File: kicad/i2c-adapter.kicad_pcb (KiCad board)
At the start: 2 copper layers, 93 x 65 mm, 41 parts, among them J1 Conn_02x13_Top_Bottom, J10 AUX IN, J11 +5V, J2 I2C-1, J3 I2C-2, J4 I2C-3R, J5 I2C-4R, J6 SPI-1, J7 SPI-2, J8 SPI-3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

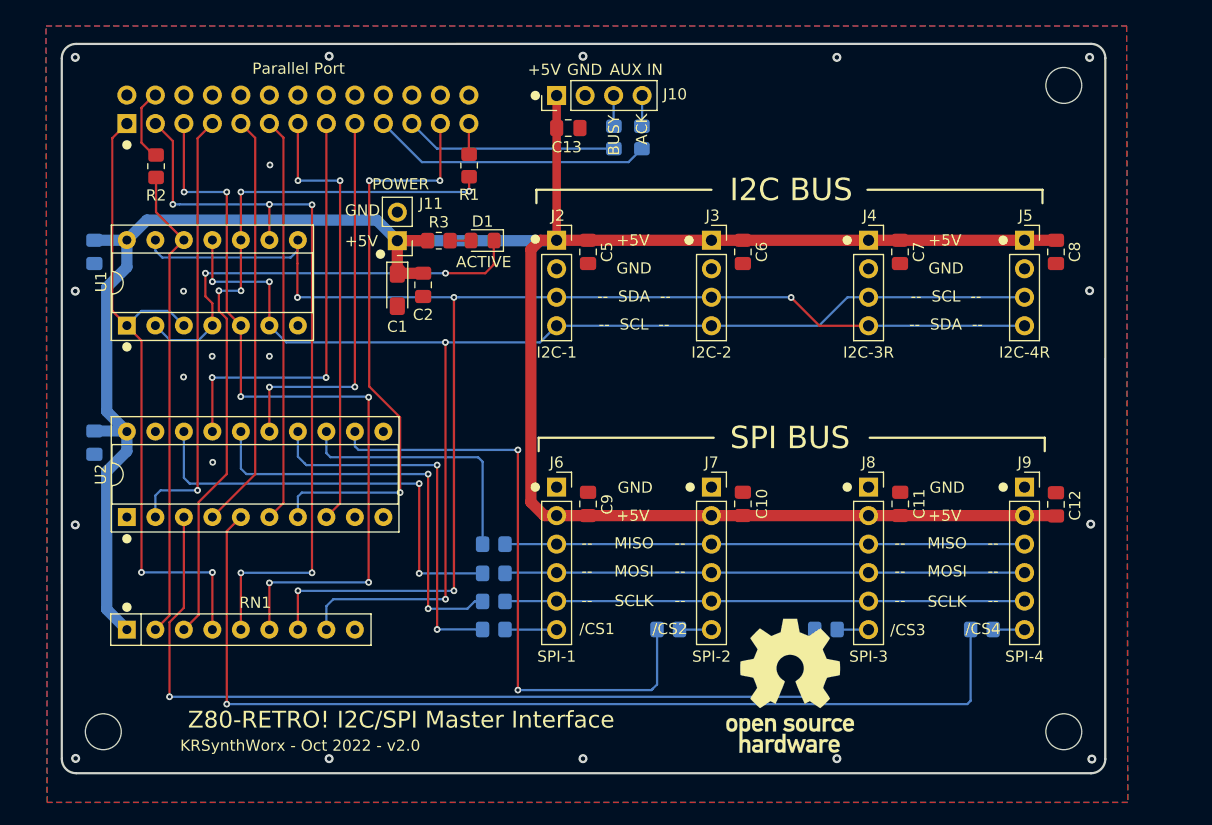
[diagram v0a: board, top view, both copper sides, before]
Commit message: Cleaned up PCB routes and positions; Converted I2C to Adafruit standard pinout. Have Git ignore Kicad generated files.
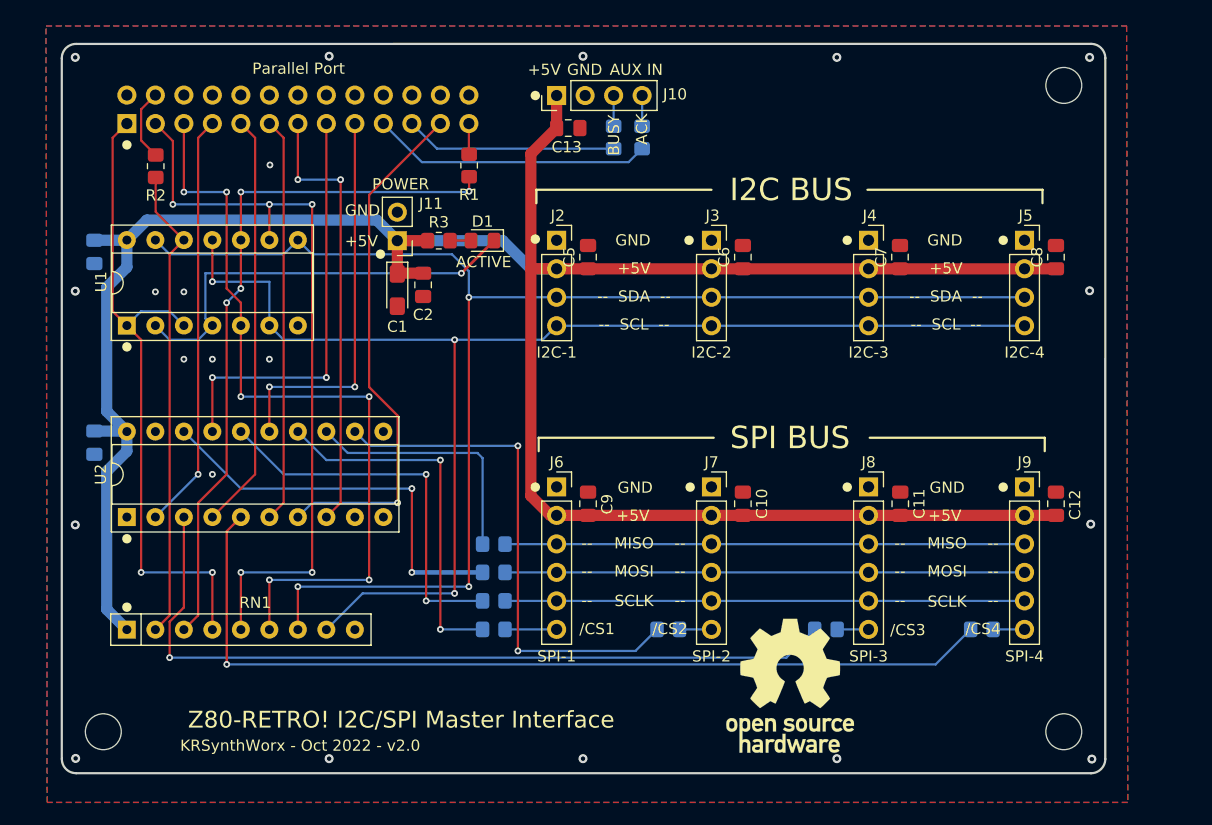
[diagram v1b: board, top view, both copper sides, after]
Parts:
- J1: footprint jb-footprint:PinSocket_2x13_P2.54mm_Vertical_clockwise -> Connector_PinSocket_2.54mm:PinSocket_2x13_P2.54mm_Vertical
- J4: value I2C-3R -> I2C-3
- J5: value I2C-4R -> I2C-4
- moved C5 0.47 mm to (147.9, 83.9), turned to 90 degrees
- moved C6 0.47 mm to (161.7, 83.9), turned to 90 degrees
- moved C7 0.47 mm to (175.7, 83.9), turned to 90 degrees
- moved C8 0.47 mm to (189.6, 83.9), turned to 90 degrees
- moved R7 0.09 mm to (139.5, 112.0)
- moved C12 0.06 mm to (189.6, 105.9)
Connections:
- J2 pad 1: +5V -> GND
- J2 pad 2: GND -> +5V
- J3 pad 1: +5V -> GND
- J3 pad 2: GND -> +5V
- J4 pad 1: +5V -> GND
- J4 pad 2: GND -> +5V
- J4 pad 3: /SCL -> /SDA
- J4 pad 4: /SDA -> /SCL
- J5 pad 1: +5V -> GND
- J5 pad 2: GND -> +5V
- J5 pad 3: /SCL -> /SDA
- J5 pad 4: /SDA -> /SCL
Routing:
- net Net-(U2-Pad5): track 90.0 -> 81.2 mm
- net Net-(U2-Pad12): track 54.9 -> 46.5 mm
- net Net-(U2-Pad3): track 79.8 -> 71.6 mm
- net /PAPER: track 51.4 -> 46.9 mm, vias 3 -> 1
- net Net-(U2-Pad16): track 37.3 -> 34.4 mm
- net +5V: track 220.5 -> 223.3 mm
- net Net-(U2-Pad18): track 39.0 -> 36.2 mm
- net /SDA: track 129.5 -> 126.8 mm, vias 5 -> 3
- net /SCL: track 118.1 -> 116.2 mm, vias 4 -> 3
- net /D2: track 39.1 -> 37.2 mm
- net Net-(R1-Pad2): track 64.5 -> 62.7 mm
- net Net-(D1-Pad1): track 39.2 -> 38.0 mm, vias 2 -> 1
- net Net-(U2-Pad14): track 33.7 -> 32.6 mm
- net Net-(U2-Pad13): track 23.5 -> 22.6 mm
- net GND: vias 20 -> 21

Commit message: Add voltage regulator for +3.3V power; Move all SMD components to top side.
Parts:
- added C14: 10uF, Capacitor_SMD:C_0805_2012Metric_Pad1.18x1.45mm_HandSolder, F.Cu at (161.7, 72.4)
- added C15: .1, Capacitor_SMD:C_0805_2012Metric_Pad1.18x1.45mm_HandSolder, F.Cu at (166.5, 75.9)
- added C16: 10uF, Capacitor_SMD:C_0805_2012Metric_Pad1.18x1.45mm_HandSolder, F.Cu at (175.7, 72.1)
- added REF1: Fiducial_0.5mm_Mask1.5mm, Fiducial:Fiducial_0.5mm_Mask1.5mm, F.Cu at (186.4, 68.6)
- added REF2: Fiducial_0.5mm_Mask1.5mm, Fiducial:Fiducial_0.5mm_Mask1.5mm, F.Cu at (108.7, 126.2)
- added U3: LM1117-3.3, digikey-footprints:SOT-223, F.Cu at (168.7, 71.1)
- C3, C4, R10, R11, R12, R4, R5, R6, R7, R8, R9: moved to F.Cu
- moved C6 1.47 mm to (162.7, 84.9), turned to 0 degrees
- moved REF** 1.34 mm to (165.9, 123.4)
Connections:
- C11 pad 1: +5V -> +3V3
- C12 pad 1: +5V -> +3V3
- C7 pad 1: +5V -> +3V3
- C8 pad 1: +5V -> +3V3
- J4 pad 2: +5V -> +3V3
- J5 pad 2: +5V -> +3V3
- J8 pad 2: +5V -> +3V3
- J9 pad 2: +5V -> +3V3
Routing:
- net +3V3: track 0.00 -> 83.6 mm
- net +5V: track 223.3 -> 185.6 mm
- net /SCL: track 116.2 -> 111.6 mm, vias 3 -> 2
- net /SDA: track 126.8 -> 123.7 mm
- net Net-(R9-Pad1): track 32.6 -> 30.7 mm, vias 2 -> 1
- net Net-(R10-Pad1): track 46.5 -> 44.7 mm, vias 2 -> 1
- net Net-(R8-Pad1): track 34.4 -> 32.9 mm, vias 2 -> 1
- net Net-(R7-Pad1): track 36.2 -> 35.1 mm, vias 2 -> 1
- net Net-(R6-Pad2): track 22.6 -> 21.7 mm, vias 0 -> 1
- net /ACK: track 25.0 -> 24.8 mm, vias 0 -> 1
- net /BUSY: vias 0 -> 1
- net Net-(R11-Pad1): vias 1 -> 0
- net GND: vias 21 -> 33
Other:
- board text added: "+3.3V"
- board text added: "KRSynthWorx - Oct 2022 - v2.1"
- board text removed: "KRSynthWorx - Oct 2022 - v2.0"

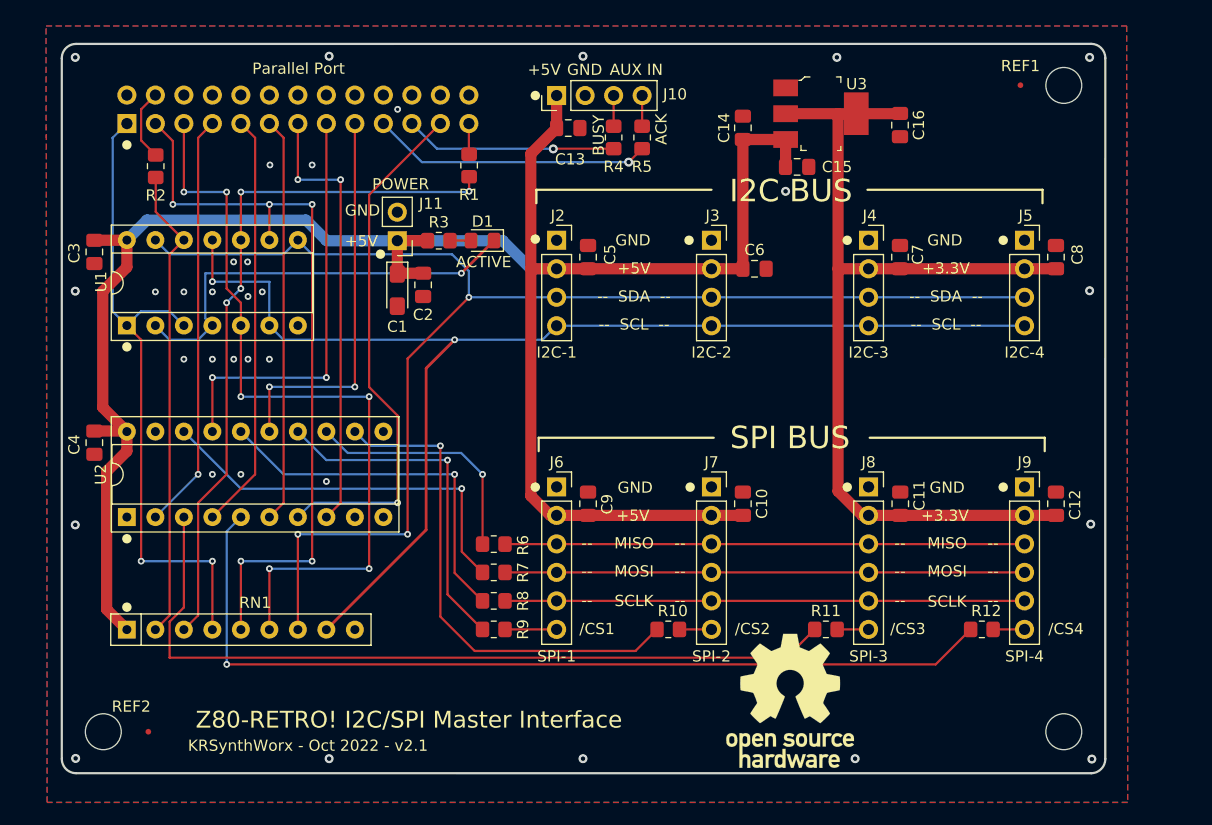
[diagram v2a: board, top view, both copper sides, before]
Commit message: Added BOM; Updated README to point to BOM Added JLCPCB SMD part references Specified LED characteristics (choose whichever color you want, default is RED) For jlcpcb/project.db, see https://github.com/Bouni/kicad-jlcpcb-tools Some minor Schematic and routing cleanups. Removed *_prl preferences file.  It is auto generated upon opening project.
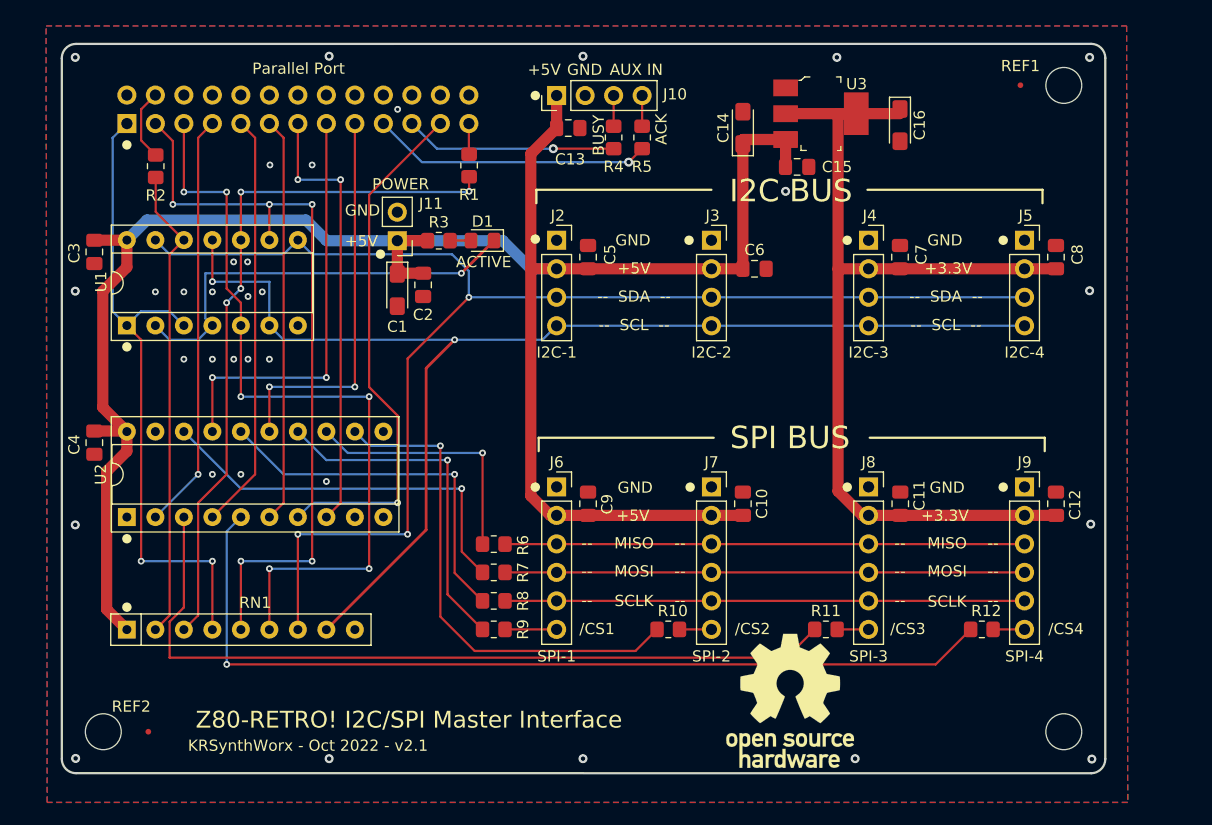
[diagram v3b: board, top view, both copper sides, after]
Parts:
- C1: value 10uf -> 10uF
- C14, C16: footprint Capacitor_SMD:C_0805_2012Metric_Pad1.18x1.45mm_HandSolder -> Capacitor_Tantalum_SMD:CP_EIA-3216-10_Kemet-I_Pad1.58x1.35mm_HandSolder
- C15: value .1 -> 0.1uF
- C2, C3, C4: value 0.1uf -> 0.1uF
- D1: value ACTIVE -> 20mA 120°
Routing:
- net Net-(R6-Pad2): track 21.7 -> 22.8 mm

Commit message: Added Adafruit compatible STEMMA QT I2C Connector and EyeSPI connector.
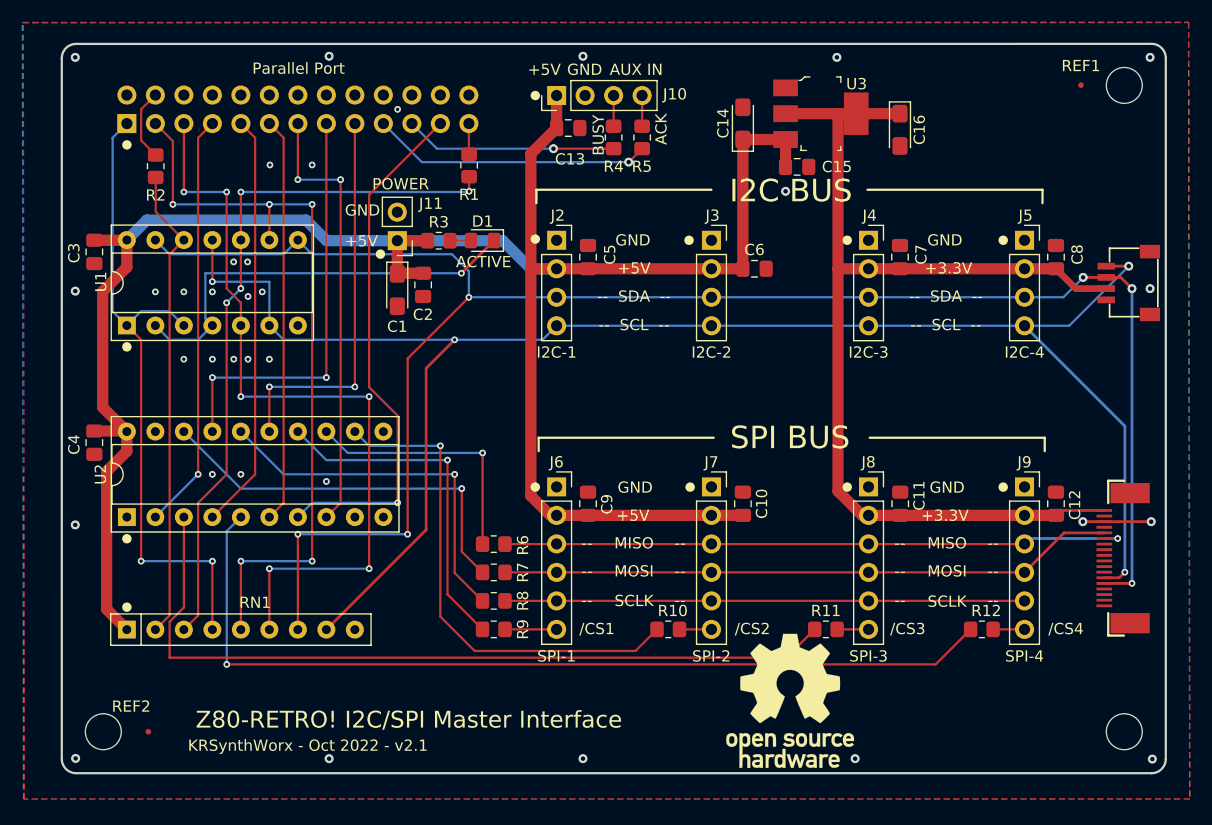
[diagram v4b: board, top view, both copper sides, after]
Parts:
- added CONN1: STEMMA_I2C_QT, i2c-adapter:JST_SH4, F.Cu at (196.6, 86.2)
- added X1: EYE_SPI_DISPLAY_FLIP, i2c-adapter:EYE_SPI_DISPLAY_BOTCONTACT, F.Cu at (195.1, 110.7)
- J1: footprint Connector_PinSocket_2.54mm:PinSocket_2x13_P2.54mm_Vertical -> i2c-adapter:PinSocket_2x13_P2.54mm_Vertical
- U3: footprint digikey-footprints:SOT-223 -> i2c-adapter:SOT-223
- moved REF1 5.39 mm to (191.8, 68.6)
- moved C16 0.42 mm to (175.7, 72.6)
- moved C14 0.40 mm to (161.7, 72.0)
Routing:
- net /SCL: track 111.6 -> 152.8 mm, vias 2 -> 4
- net /SDA: track 123.7 -> 163.1 mm, vias 3 -> 6
- net /MISO: track 46.3 -> 56.0 mm, vias 0 -> 1
- net +3V3: track 83.6 -> 93.3 mm
- net /MOSI: track 46.3 -> 54.9 mm
- net GND: track 0.00 -> 6.09 mm, vias 33 -> 34
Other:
- board size 93 x 65 mm -> 98.4 x 65 mm
